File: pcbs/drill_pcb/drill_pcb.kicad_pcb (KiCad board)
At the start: 2 copper layers, 105 x 103 mm, 31 parts, among them J1 24V IN, J10 WEIGHT SENSOR, J11 STEPPER STORAGE, J2 DC MOTOR 24 V, J3 DC MOTOR UART, J4 ENCODER VERTICAL DRIVE, J5 LIMIT SENSOR TOP, J6 HEIGHT SENSOR, J7 STEPPER VERTICAL DRIVE, J8 ENCODER STORAGE, J9 LIMIT SENSOR BOTTOM, U1 ESP32-DevKitC, U2 LM3940

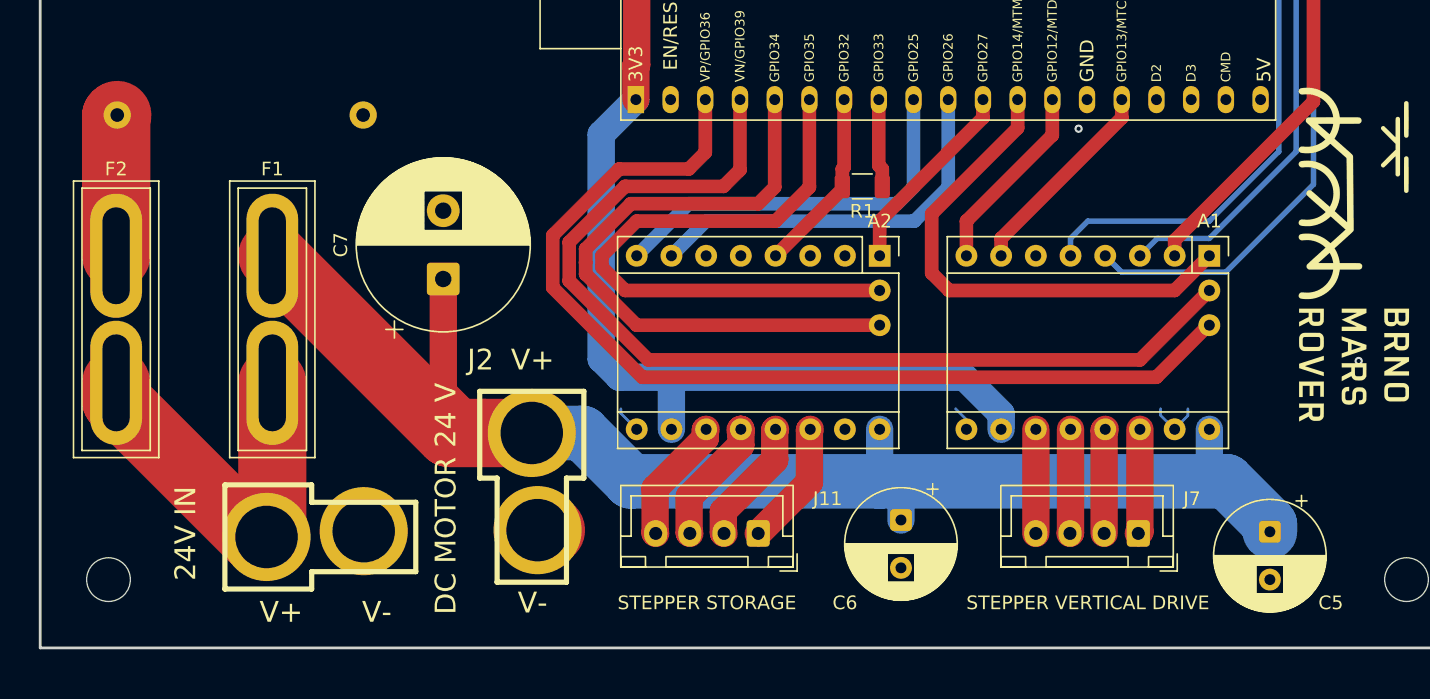
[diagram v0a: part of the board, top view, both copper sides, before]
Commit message: finished new fuse holder library. PCB tweaks.
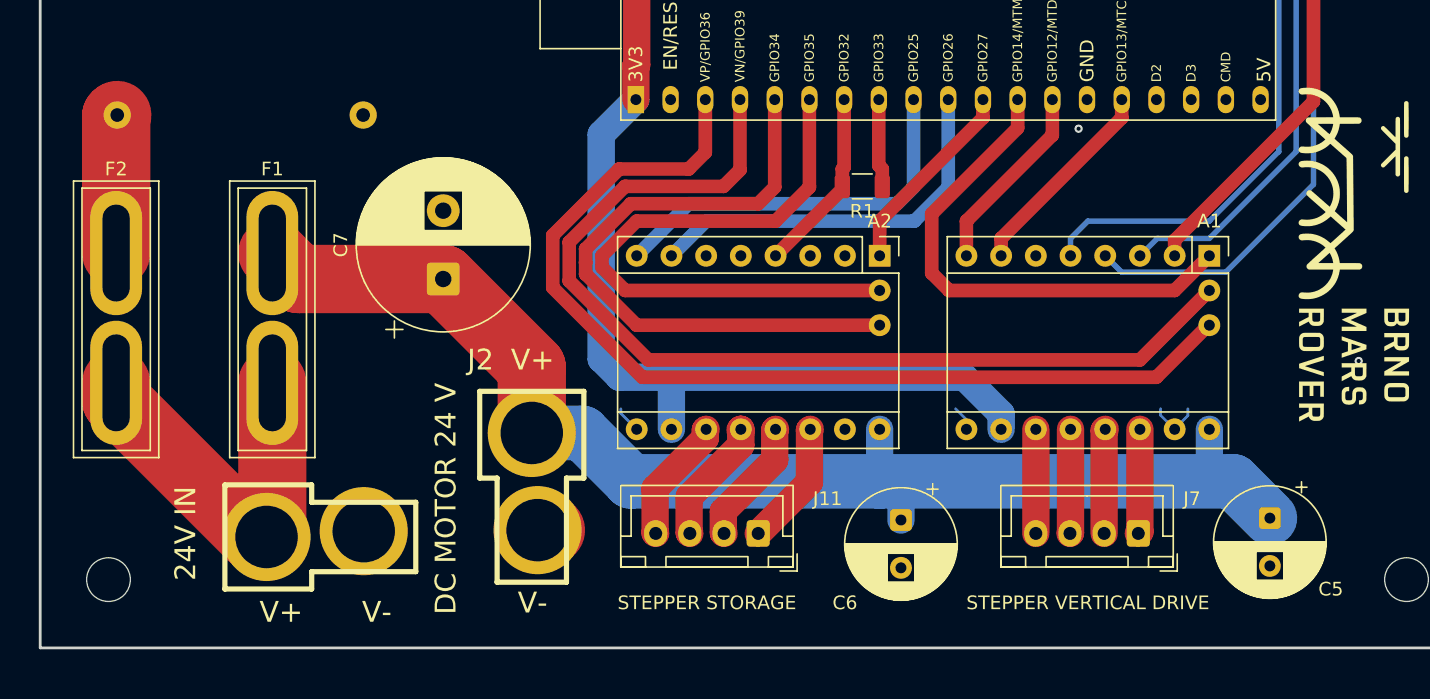
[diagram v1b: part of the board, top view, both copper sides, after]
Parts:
- F1, F2: footprint drill_fuseSlot:fuseSlot -> drill_fuseHolderATO:fuseHolderATO
- moved C5 1.00 mm to (120.0, 133.5)
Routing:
- net +24V: track 106.1 -> 100.0 mm
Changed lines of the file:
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@@
 		)
 	)
-	(footprint "drill_fuseSlot:fuseSlot"
+	(footprint "drill_fuseHolderATO:fuseHolderATO"
 		(layer "F.Cu")
 		(at 46.99 123.6 90)
@@
 		)
 		(pad "2" thru_hole oval
-			(at 9.3 0 90)
+			(at 9.5 0 90)
 			(size 9.1 3.8)
 			(drill oval 7.1 2)
@@
 	(footprint "Capacitor_THT:CP_Radial_D8.0mm_P3.50mm"
 		(layer "F.Cu")
-		(at 120 134.5 -90)
+		(at 120 133.5 -90)
 		(descr "CP, Radial series, Radial, pin pitch=3.50mm, diameter=8mm, height=12mm, Electrolytic Capacitor")
 		(tags "CP Radial series Radial pin pitch 3.50mm diameter 8mm height 12mm Electrolytic Capacitor")
@@
 		)
 	)
-	(footprint "drill_fuseSlot:fuseSlot"
+	(footprint "drill_fuseHolderATO:fuseHolderATO"
 		(layer "F.Cu")
 		(at 35.56 123.6 90)
@@
 		)
 		(pad "2" thru_hole oval
-			(at 9.3 0 90)
+			(at 9.5 0 90)
 			(size 9.1 3.8)
 			(drill oval 7.1 2)
@@
 	)
 	(segment
-		(start 59.5 124.268)
-		(end 62.5 127.268)
-		(width 2)
-		(layer "F.Cu")
-		(net 3)
-	)
-	(segment
-		(start 59.5 116)
-		(end 59.5 124.268)
-		(width 2)
+		(start 48.89 116)
+		(end 59.5 116)
+		(width 5)
 		(layer "F.Cu")
 		(net 3)
 	)
 	(segment
-		(start 59.958 127.268)
-		(end 46.99 114.3)
+		(start 65.98 122.48)
+		(end 59.5 116)
 		(width 5)
 		(layer "F.Cu")
@@
 	)
 	(segment
-		(start 62.5 127.268)
-		(end 65.98 127.268)
+		(start 65.98 127.268)
+		(end 65.98 122.48)
 		(width 5)
 		(layer "F.Cu")
@@
 	)
 	(segment
-		(start 62.5 127.268)
-		(end 59.958 127.268)
+		(start 46.99 114.1)
+		(end 48.89 116)
 		(width 5)
 		(layer "F.Cu")
@@
 	)
 	(segment
-		(start 115.57 129.54)
-		(end 116.84 130.81)
+		(start 120 133.5)
+		(end 119.5 133)
 		(width 2)
 		(layer "B.Cu")
@@
 	)
 	(segment
-		(start 69.683945 127.268)
-		(end 73.225945 130.81)
-		(width 4)
+		(start 119.5 133)
+		(end 119.03 133)
+		(width 2)
 		(layer "B.Cu")
 		(net 3)
 	)
 	(segment
-		(start 116.84 130.81)
-		(end 120 133.97)
-		(width 4)
+		(start 115.57 129.54)
+		(end 115.57 127)
+		(width 2)
 		(layer "B.Cu")
 		(net 3)
 	)
 	(segment
-		(start 120 133.97)
-		(end 120 134.5)
+		(start 69.683945 127.268)
+		(end 73.225945 130.81)
 		(width 4)
 		(layer "B.Cu")
@@
 	)
 	(segment
-		(start 91.44 130.81)
-		(end 116.84 130.81)
-		(width 4)
-		(layer "B.Cu")
-		(net 3)
-	)
-	(segment
 		(start 93 132.37)
 		(end 91.44 130.81)
@@
 	)
 	(segment
-		(start 65.98 127.268)
-		(end 66.164 127.084)
+		(start 117.31 130.81)
+		(end 91.44 130.81)
 		(width 4)
 		(layer "B.Cu")
@@
 	)
 	(segment
-		(start 115.57 127)
-		(end 115.57 129.54)
-		(width 2)
+		(start 65.98 127.268)
+		(end 66.164 127.084)
+		(width 4)
 		(layer "B.Cu")
 		(net 3)
@@
 	)
 	(segment
+		(start 119.03 133)
+		(end 115.57 129.54)
+		(width 2)
+		(layer "B.Cu")
+		(net 3)
+	)
+	(segment
+		(start 120 133.5)
+		(end 117.31 130.81)
+		(width 4)
+		(layer "B.Cu")
+		(net 3)
+	)
+	(segment
 		(start 65.98 127.268)
 		(end 69.683945 127.268)
@@
 	)
 	(segment
-		(start 46.99 134.458)
-		(end 46.568 134.88)
+		(start 45.57 134.88)
+		(end 35.56 124.87)
 		(width 5)
 		(layer "F.Cu")
@@
 	)
 	(segment
-		(start 45.57 134.88)
-		(end 35.56 124.87)
+		(start 46.99 134.458)
+		(end 46.568 134.88)
 		(width 5)
 		(layer "F.Cu")
@@
 	)
 	(segment
-		(start 35.56 104.08)
-		(end 35.64 104)
+		(start 35.56 114.1)
+		(end 35.56 104.08)
 		(width 5)
 		(layer "F.Cu")
@@
 	)
 	(segment
-		(start 35.56 114.3)
-		(end 35.56 104.08)
+		(start 35.56 104.08)
+		(end 35.64 104)
 		(width 5)
 		(layer "F.Cu")

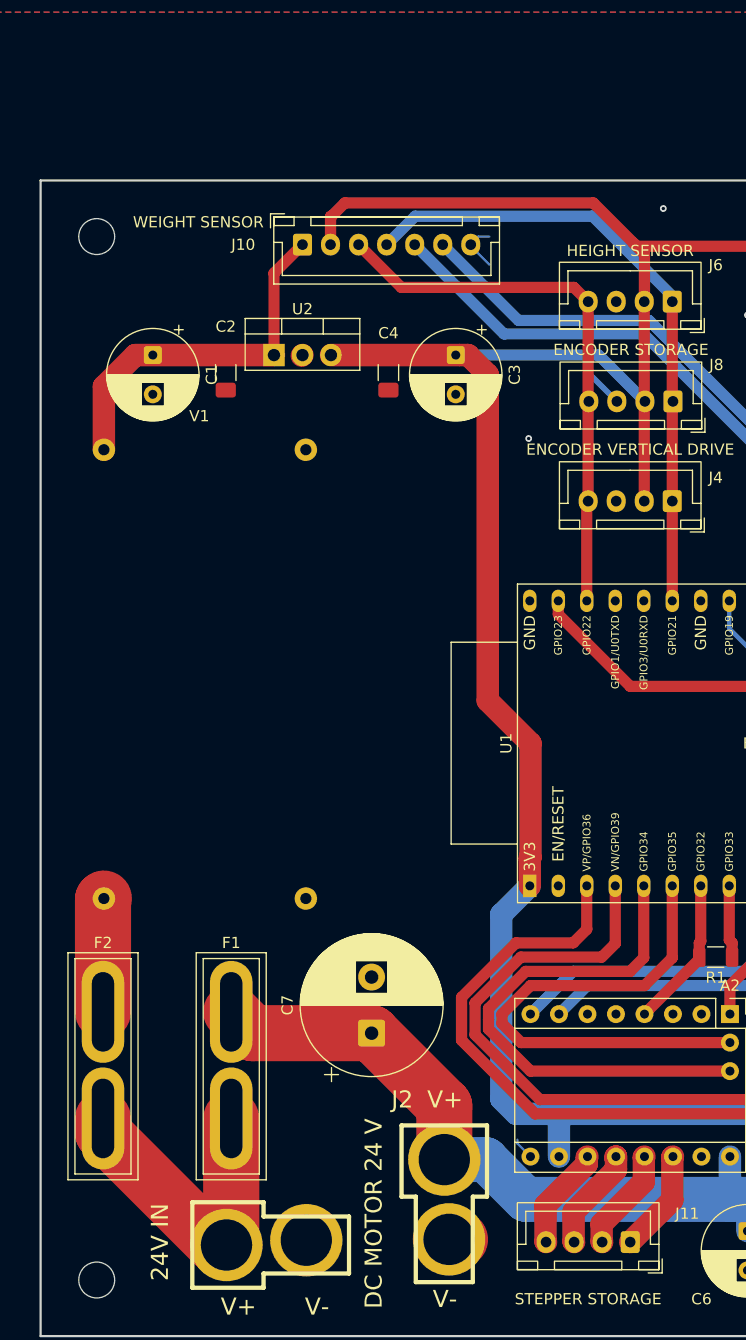
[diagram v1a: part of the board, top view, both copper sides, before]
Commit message: Cloned last version of PCB to preserve documentation for already manufactured hardware. New version of PCB includes connector for surface sample weighing, UART0 JST connector, I2C pullup resistors, new fuse footprint
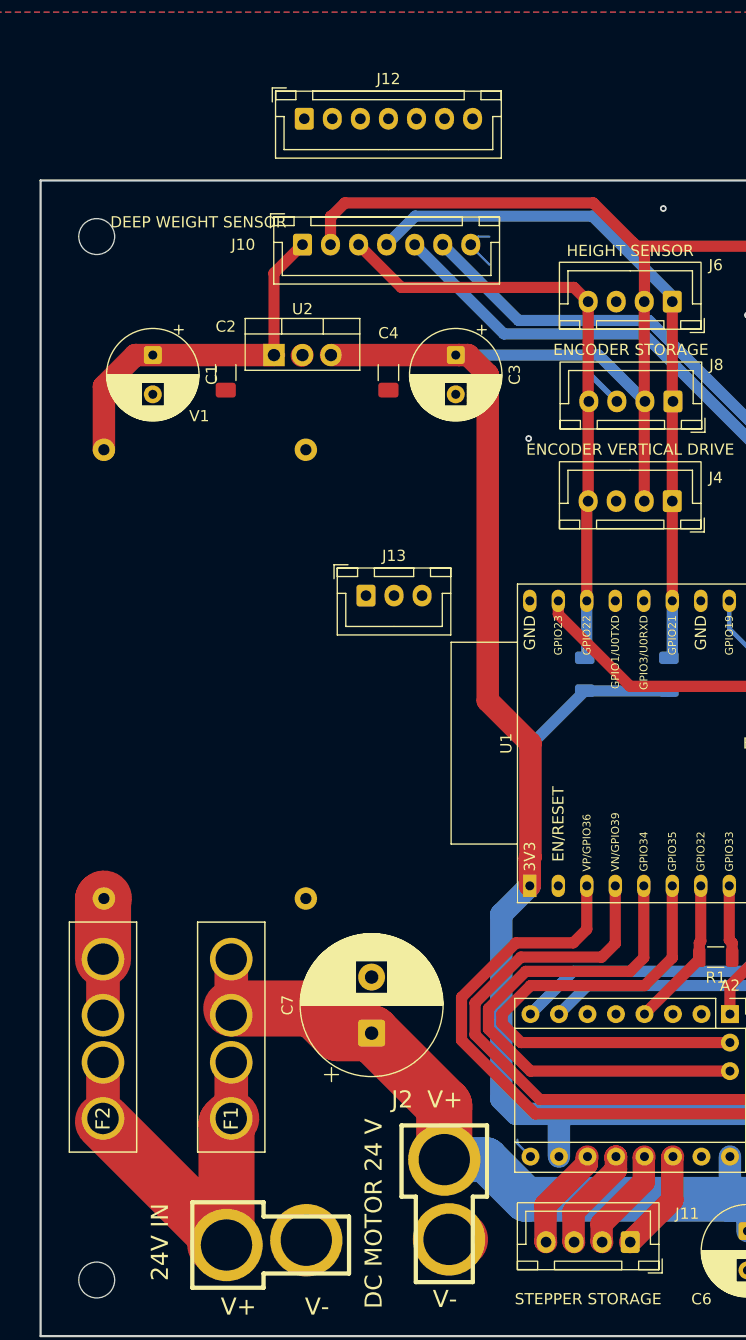
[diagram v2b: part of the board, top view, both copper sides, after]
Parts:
- added J12: SURFACE WEIGHT SENSOR, Connector_JST:JST_XH_B7B-XH-A_1x07_P2.50mm_Vertical, F.Cu at (53.5, 34.5)
- added J13: uC COMMUNICATION, Connector_JST:JST_XH_B3B-XH-A_1x03_P2.50mm_Vertical, F.Cu at (59.0, 77.0)
- added R2: 2200, Resistor_SMD:R_1206_3216Metric, B.Cu at (86.0, 84.0)
- added R3: 2200, Resistor_SMD:R_1206_3216Metric, B.Cu at (78.5, 84.0)
- F1, F2: footprint drill_fuseHolderATO:fuseHolderATO -> drill_fuseHolderATO:AUTOFUSE_HOLDER
- J10: value WEIGHT SENSOR -> DEEP WEIGHT SENSOR
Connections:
- net ADC_DRDY renamed ADC_DEEP_DRDY
- net ADC_RST renamed ADC_DEEP_RST
- U1 pad 34: unconnected-(U1-U0RXD/GPIO3-Pad34) -> RX0
- U1 pad 35: unconnected-(U1-U0TXD/GPIO1-Pad35) -> TX0
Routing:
- net +3.3V: track 244.1 -> 271.1 mm
- net Net-(J1-Pin_1): track 27.9 -> 38.6 mm
- net SDA1: track 56.6 -> 61.8 mm
- net SCL1: track 49.4 -> 54.5 mm
- net +24V: track 100.0 -> 105.1 mm

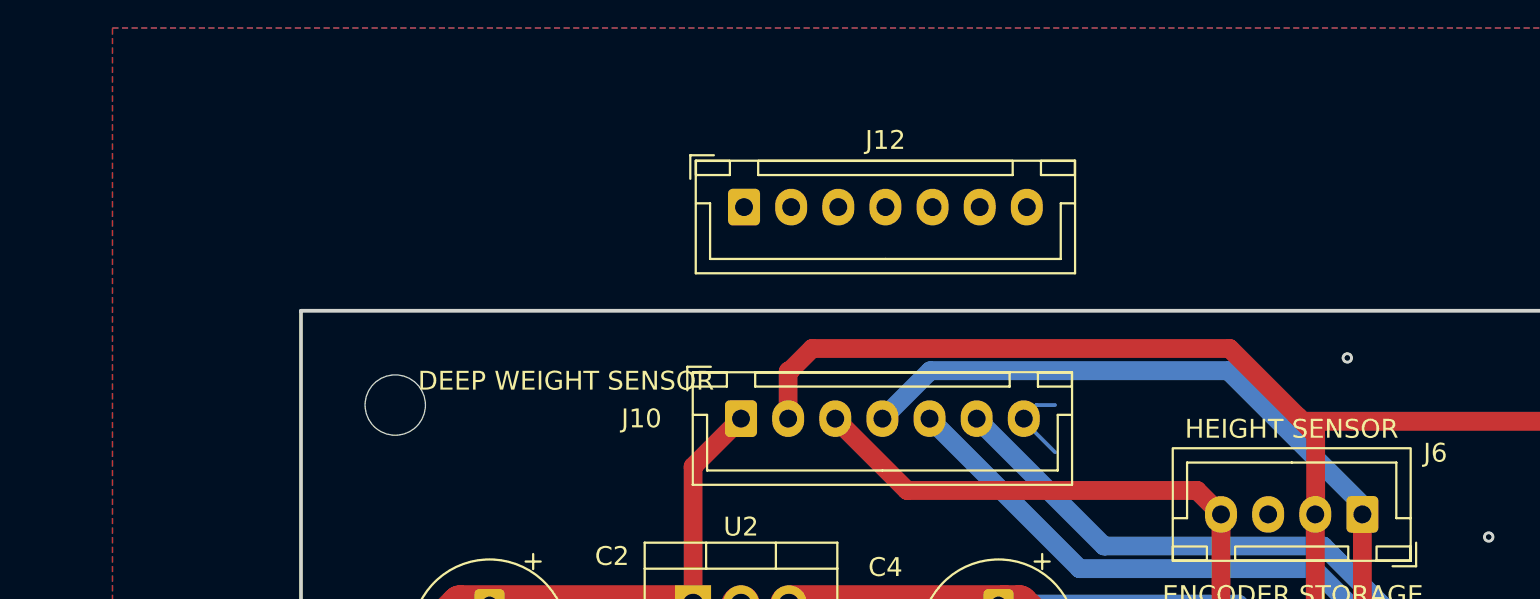
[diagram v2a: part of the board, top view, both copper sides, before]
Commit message: ADC redundant 3/4 pins deleted
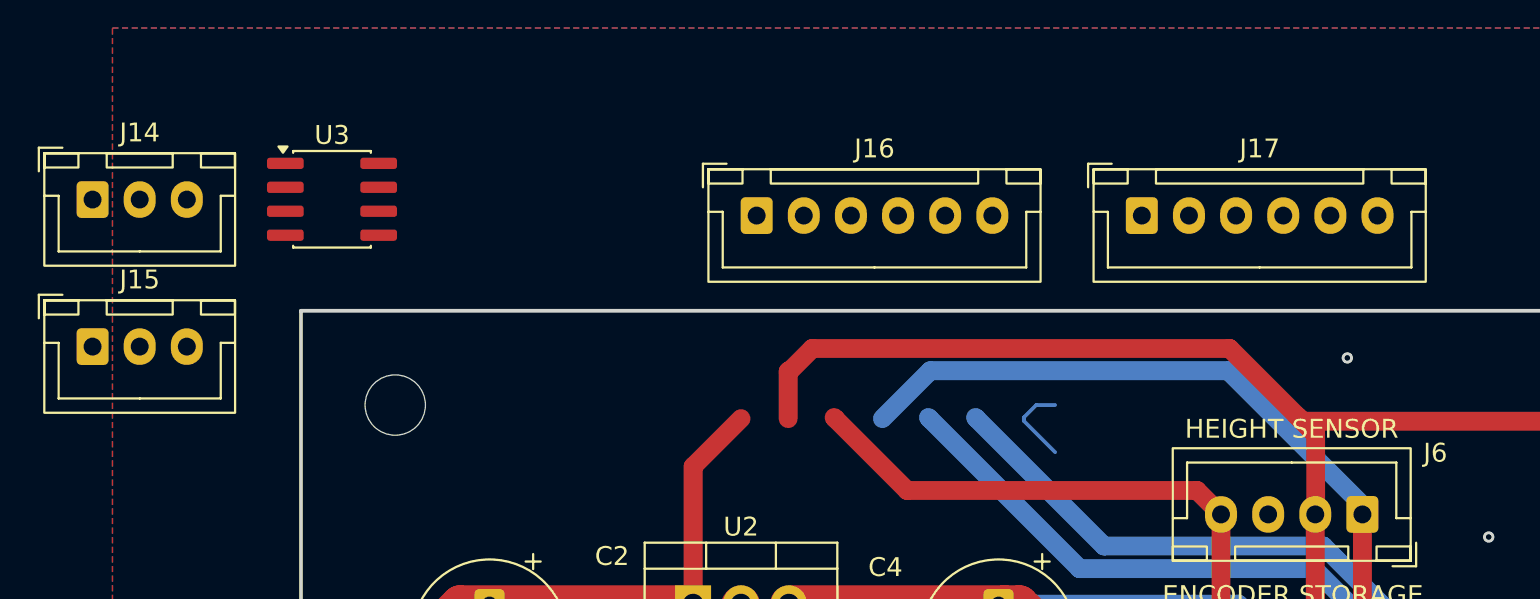
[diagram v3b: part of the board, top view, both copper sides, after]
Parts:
- removed J10: DEEP WEIGHT SENSOR, Connector_JST:JST_XH_B7B-XH-A_1x07_P2.50mm_Vertical
- removed J12: SURFACE WEIGHT SENSOR, Connector_JST:JST_XH_B7B-XH-A_1x07_P2.50mm_Vertical
- added J14: SERVO 1, Connector_JST:JST_XH_B3B-XH-A_1x03_P2.50mm_Vertical, F.Cu at (18.9, 34.1)
- added J15: SERVO 2, Connector_JST:JST_XH_B3B-XH-A_1x03_P2.50mm_Vertical, F.Cu at (18.9, 41.9)
- added J16: DEEP WEIGHT SENSOR, Connector_JST:JST_XH_B6B-XH-A_1x06_P2.50mm_Vertical, F.Cu at (54.2, 35.0)
- added J17: SURFACE WEIGHT SENSOR, Connector_JST:JST_XH_B6B-XH-A_1x06_P2.50mm_Vertical, F.Cu at (74.6, 35.0)
- added U3: INA219BxD, Package_SO:SOIC-8_3.9x4.9mm_P1.27mm, F.Cu at (31.6, 34.1)
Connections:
- A2 pad 17: DRVR_STORAGE_0 -> unconnected-(A2-DIAG0-Pad17)
- A2 pad 18: DRVR_STORAGE_1 -> unconnected-(A2-DIAG1-Pad18)
- U1 pad 23: LIMIT_SENSOR_TOP -> unconnected-(U1-MTDO/GPIO15/ADC2_CH3-Pad23)
- U1 pad 25: LIMIT_SENSOR_BOTTOM -> unconnected-(U1-GPIO0/BOOT/ADC2_CH1-Pad25)
- U1 pad 26: ADC_DEEP_DRDY -> unconnected-(U1-ADC2_CH0/GPIO4-Pad26)
- U1 pad 5: DRVR_STORAGE_1 -> LIMIT_SENSOR_BOTTOM
- U1 pad 6: DRVR_STORAGE_0 -> LIMIT_SENSOR_TOP
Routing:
- net unconnected-(U1-ADC2_CH0/GPIO4-Pad26): track 0.00 -> 56.0 mm
- net ADC_DEEP_DRDY: track 56.0 -> 0.00 mm
- net LIMIT_SENSOR_BOTTOM: track 8.91 -> 55.9 mm
- net DRVR_STORAGE_1: track 47.0 -> 0.00 mm
- net LIMIT_SENSOR_TOP: track 19.9 -> 65.4 mm
- net DRVR_STORAGE_0: track 45.5 -> 0.00 mm

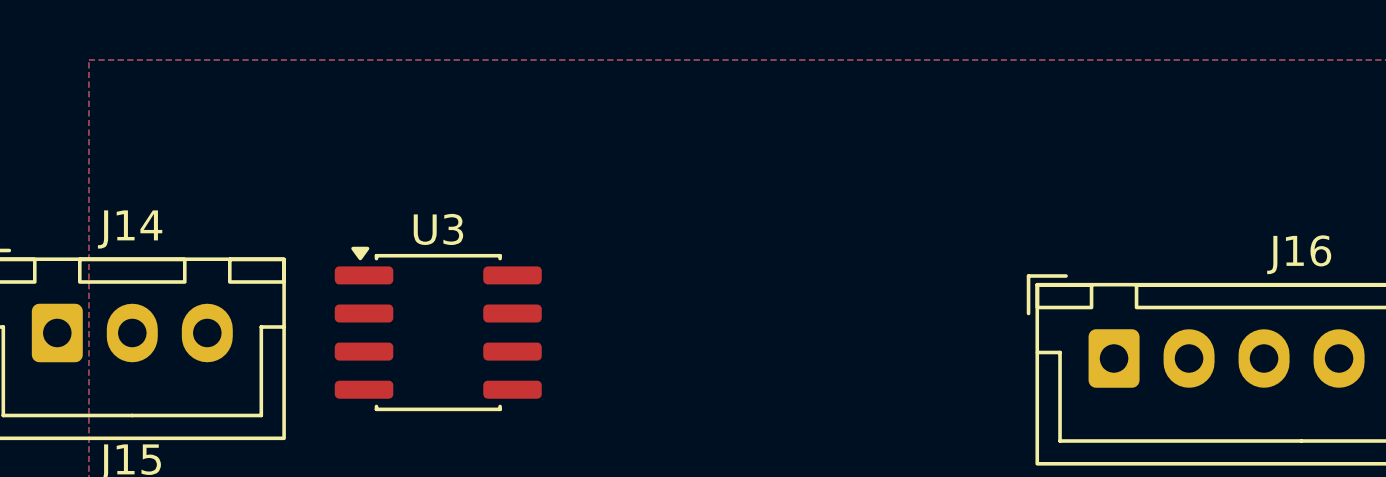
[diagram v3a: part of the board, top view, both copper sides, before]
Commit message: single RST MOSFET added
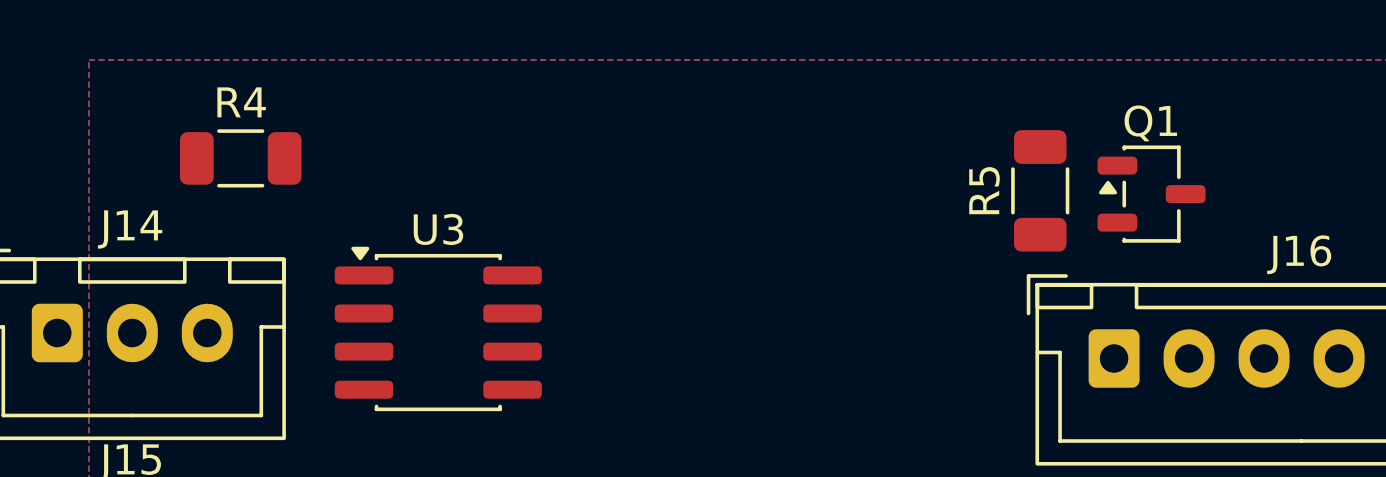
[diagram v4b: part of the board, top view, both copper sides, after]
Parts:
- added Q1: PMOS, Package_TO_SOT_SMD:SOT-23-3, F.Cu at (55.4, 29.5)
- added R4: R, Resistor_SMD:R_1206_3216Metric, F.Cu at (25.1, 28.3)
- added R5: R, Resistor_SMD:R_1206_3216Metric, F.Cu at (51.7, 29.4)
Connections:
- J16 pad 2: +3.3V -> Net-(J16-Pin_2)
- J17 pad 2: +3.3V -> Net-(J16-Pin_2)
